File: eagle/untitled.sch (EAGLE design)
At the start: 58 parts, among them J1 JTAG, Q1 16MHz, U1 MMA3202KEG

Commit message: 2nd version in production.
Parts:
- BOOST: value V_REG_TPS61040SMD -> TPS61040
- D13: value DIODE -> MBRA140; device gipi:DIODE -> SparkFun-DiscreteSemi:DIODE-SCHOTTKY-MBRA140
- L1: value (none) -> 3.3uH; device SparkFun-Passives:INDUCTOR0603 -> SparkFun-Passives:INDUCTOR1210
- N-FET: value P-CHANNEL-MOSFET -> N-CHANNEL-MOSFET-BSS138; device GeekAmmo:P-CHANNEL-MOSFET -> GeekAmmo:N-CHANNEL-MOSFET-BSS138
- RA: value 1k -> 3.09k
- renumbered R17 to RA, R18 to RB
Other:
- moved on the sheet: N-FET
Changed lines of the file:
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@@
 <part name="XS" library="SparkFun-LED" deviceset="LED" device="0603"/>
 <part name="GND-ISO13" library="SparkFun-Aesthetics" deviceset="GND-ISO" device=""/>
-<part name="BOOST" library="SparkFun-PowerIC" deviceset="V_REG_TPS61040" device="SMD"/>
-<part name="L1" library="SparkFun-Passives" deviceset="INDUCTOR" device="0603"/>
+<part name="BOOST" library="SparkFun-PowerIC" deviceset="V_REG_TPS61040" device="SMD" value="TPS61040"/>
+<part name="L1" library="SparkFun-Passives" deviceset="INDUCTOR" device="1210" value="3.3uH"/>
 <part name="C7" library="SparkFun-Capacitors" deviceset="CAP" device="0603-CAP" value="10nF"/>
 <part name="GND-ISO14" library="SparkFun-Aesthetics" deviceset="GND-ISO" device=""/>
-<part name="D13" library="gipi" deviceset="DIODE" device=""/>
-<part name="R17" library="SparkFun-Passives" deviceset="RESISTOR" device="0603-RES" value="1k"/>
-<part name="R18" library="SparkFun-Passives" deviceset="RESISTOR" device="0603-RES" value="1k"/>
+<part name="D13" library="SparkFun-DiscreteSemi" deviceset="DIODE-SCHOTTKY" device="-MBRA140" value="MBRA140"/>
+<part name="RA" library="SparkFun-Passives" deviceset="RESISTOR" device="0603-RES" value="3.09k"/>
+<part name="RB" library="SparkFun-Passives" deviceset="RESISTOR" device="0603-RES" value="1k"/>
 <part name="C8" library="SparkFun-Capacitors" deviceset="CAP" device="0603-CAP" value="10nF"/>
 <part name="C9" library="SparkFun-Capacitors" deviceset="CAP" device="0603-CAP" value="10nF"/>
@@
 <part name="GND-ISO2" library="SparkFun-Aesthetics" deviceset="GND-ISO" device=""/>
 <part name="JP6" library="SparkFun-Connectors" deviceset="M02" device="JST-PTH-VERT"/>
-<part name="N-FET" library="GeekAmmo" deviceset="P-CHANNEL-MOSFET" device=""/>
+<part name="N-FET" library="GeekAmmo" deviceset="N-CHANNEL-MOSFET" device="-BSS138"/>
 <part name="TP1" library="gipi" deviceset="TESTPAD" device=""/>
 </parts>
@@
 <instance part="GND-ISO14" gate="G$1" x="88.9" y="-246.38"/>
 <instance part="D13" gate="G$1" x="71.12" y="-205.74"/>
-<instance part="R17" gate="G$1" x="81.28" y="-215.9" rot="R90"/>
-<instance part="R18" gate="G$1" x="76.2" y="-233.68" rot="R90"/>
+<instance part="RA" gate="G$1" x="81.28" y="-215.9" rot="R90"/>
+<instance part="RB" gate="G$1" x="76.2" y="-233.68" rot="R90"/>
 <instance part="C8" gate="G$1" x="99.06" y="-213.36" rot="R180"/>
 <instance part="C9" gate="G$1" x="114.3" y="-226.06" rot="R180"/>
@@
 <instance part="GND-ISO2" gate="G$1" x="-33.02" y="20.32"/>
 <instance part="JP6" gate="G$1" x="-27.94" y="-208.28" rot="R270"/>
-<instance part="N-FET" gate="G$1" x="-15.24" y="-220.98" rot="R90"/>
+<instance part="N-FET" gate="G$1" x="-7.62" y="-228.6"/>
 <instance part="TP1" gate="G$1" x="38.1" y="-134.62" rot="R180"/>
 </instances>
@@
 <wire x1="10.16" y1="-215.9" x2="10.16" y2="-223.52" width="0.1524" layer="91"/>
 <junction x="10.16" y="-215.9"/>
-<wire x1="-5.08" y1="-218.44" x2="-5.08" y2="-205.74" width="0.1524" layer="91"/>
+<wire x1="-5.08" y1="-220.98" x2="-5.08" y2="-205.74" width="0.1524" layer="91"/>
 <wire x1="-5.08" y1="-205.74" x2="10.16" y2="-205.74" width="0.1524" layer="91"/>
 <junction x="10.16" y="-205.74"/>
 <pinref part="N-FET" gate="G$1" pin="D"/>
-<wire x1="-7.62" y1="-218.44" x2="-5.08" y2="-218.44" width="0.1524" layer="91"/>
 </segment>
 </net>
@@
 <wire x1="63.5" y1="-220.98" x2="63.5" y2="-241.3" width="0.1524" layer="91"/>
 <junction x="63.5" y="-241.3"/>
-<pinref part="R18" gate="G$1" pin="1"/>
+<pinref part="RB" gate="G$1" pin="1"/>
 <wire x1="76.2" y1="-238.76" x2="76.2" y2="-241.3" width="0.1524" layer="91"/>
 <junction x="76.2" y="-241.3"/>
@@
 <wire x1="114.3" y1="-241.3" x2="114.3" y2="-231.14" width="0.1524" layer="91"/>
 <junction x="88.9" y="-241.3"/>
-<wire x1="-25.4" y1="-241.3" x2="-17.78" y2="-241.3" width="0.1524" layer="91"/>
+<wire x1="-25.4" y1="-241.3" x2="-12.7" y2="-241.3" width="0.1524" layer="91"/>
 <junction x="10.16" y="-241.3"/>
 <pinref part="JP6" gate="G$1" pin="2"/>
-<wire x1="-17.78" y1="-241.3" x2="10.16" y2="-241.3" width="0.1524" layer="91"/>
+<wire x1="-12.7" y1="-241.3" x2="10.16" y2="-241.3" width="0.1524" layer="91"/>
 <wire x1="-25.4" y1="-215.9" x2="-25.4" y2="-241.3" width="0.1524" layer="91"/>
 <pinref part="N-FET" gate="G$1" pin="G"/>
-<wire x1="-17.78" y1="-226.06" x2="-17.78" y2="-241.3" width="0.1524" layer="91"/>
-<junction x="-17.78" y="-241.3"/>
+<wire x1="-12.7" y1="-231.14" x2="-12.7" y2="-241.3" width="0.1524" layer="91"/>
+<junction x="-12.7" y="-241.3"/>
 </segment>
 <segment>
@@
 <pinref part="BOOST" gate="G$1" pin="FB"/>
 <wire x1="45.72" y1="-226.06" x2="76.2" y2="-226.06" width="0.1524" layer="91"/>
-<pinref part="R18" gate="G$1" pin="2"/>
+<pinref part="RB" gate="G$1" pin="2"/>
 <wire x1="76.2" y1="-226.06" x2="81.28" y2="-226.06" width="0.1524" layer="91"/>
 <wire x1="81.28" y1="-226.06" x2="99.06" y2="-226.06" width="0.1524" layer="91"/>
 <wire x1="76.2" y1="-228.6" x2="76.2" y2="-226.06" width="0.1524" layer="91"/>
 <junction x="76.2" y="-226.06"/>
-<pinref part="R17" gate="G$1" pin="1"/>
+<pinref part="RA" gate="G$1" pin="1"/>
 <wire x1="81.28" y1="-220.98" x2="81.28" y2="-226.06" width="0.1524" layer="91"/>
 <junction x="81.28" y="-226.06"/>
@@
 <pinref part="D13" gate="G$1" pin="C"/>
 <wire x1="99.06" y1="-205.74" x2="81.28" y2="-205.74" width="0.1524" layer="91"/>
-<pinref part="R17" gate="G$1" pin="2"/>
+<pinref part="RA" gate="G$1" pin="2"/>
 <wire x1="81.28" y1="-205.74" x2="73.66" y2="-205.74" width="0.1524" layer="91"/>
 <wire x1="81.28" y1="-210.82" x2="81.28" y2="-205.74" width="0.1524" layer="91"/>
@@
 <segment>
 <pinref part="JP6" gate="G$1" pin="1"/>
-<wire x1="-27.94" y1="-215.9" x2="-27.94" y2="-218.44" width="0.1524" layer="91"/>
+<wire x1="-27.94" y1="-215.9" x2="-27.94" y2="-236.22" width="0.1524" layer="91"/>
 <pinref part="N-FET" gate="G$1" pin="S"/>
-<wire x1="-27.94" y1="-218.44" x2="-22.86" y2="-218.44" width="0.1524" layer="91"/>
-</segment>
-</net>
+<wire x1="-27.94" y1="-236.22" x2="-5.08" y2="-236.22" width="0.1524" layer="91"/>
+</segment>
+</net>

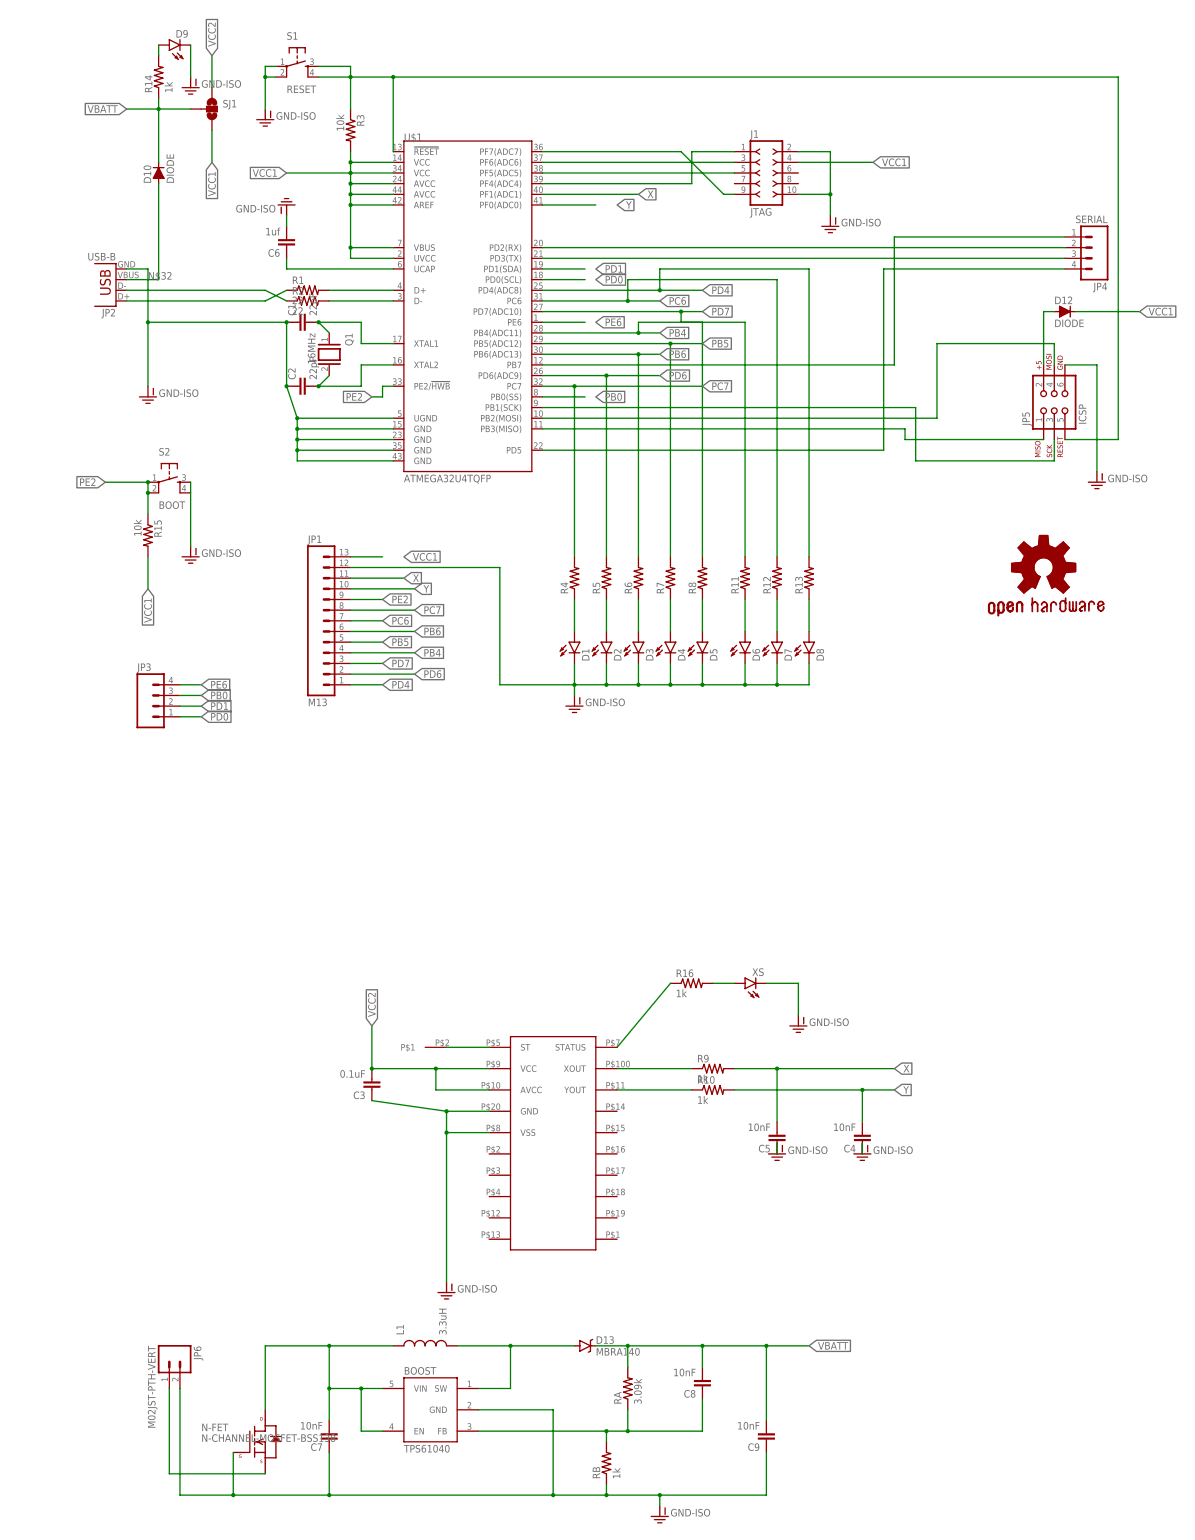
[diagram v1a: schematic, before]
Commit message: Fix mess with ground.
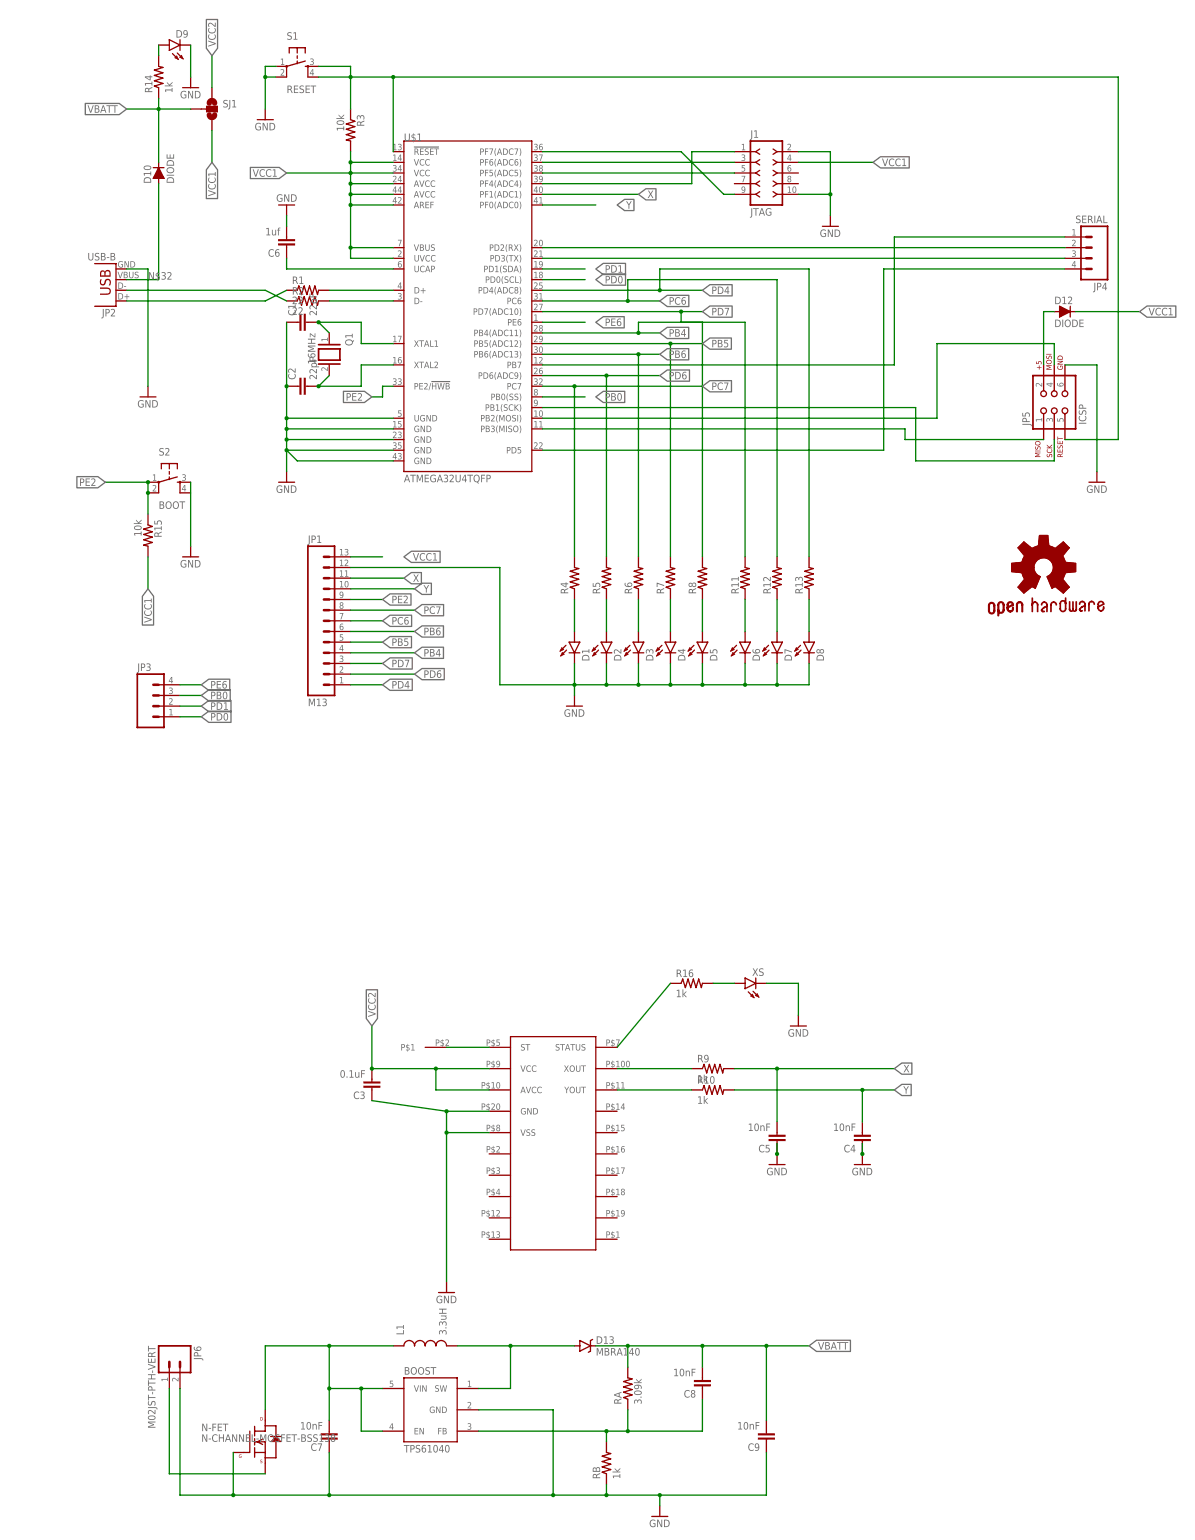
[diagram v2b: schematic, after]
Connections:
- removed net GN: C4.1, C5.1, C6.2, D1.C, D2.C, D3.C, D4.C, D5.C, D6.C, D7.C, D8.C, D9.C, J1.10, J1.2, JP1.12, JP5.6, S1.1, S1.2, S2.3, XS.C
- removed net GND-ISO: BOOST.GND, C1.1, C2.1, C3.1, C7.1, C9.1, JP2.GND, JP6.2, N-FET.G, RB.1, U$1.GND@15, U$1.GND@23, U$1.GND@35, U$1.GND@43, U$1.UGND, U1.GND, U1.VSS
- new net GND: BOOST.GND, C1.1, C2.1, C3.1, C4.1, C5.1, C6.2, C7.1, C9.1, D1.C, D2.C, D3.C, D4.C, D5.C, D6.C, D7.C, D8.C, D9.C, J1.10, J1.2, JP1.12, JP2.GND, JP5.6, JP6.2, N-FET.G, RB.1, S1.1, S1.2, S2.3, U$1.GND@15, U$1.GND@23, U$1.GND@35, U$1.GND@43, U$1.UGND, U1.GND, U1.VSS, XS.C

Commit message: Update ciaoduino's eagle files.
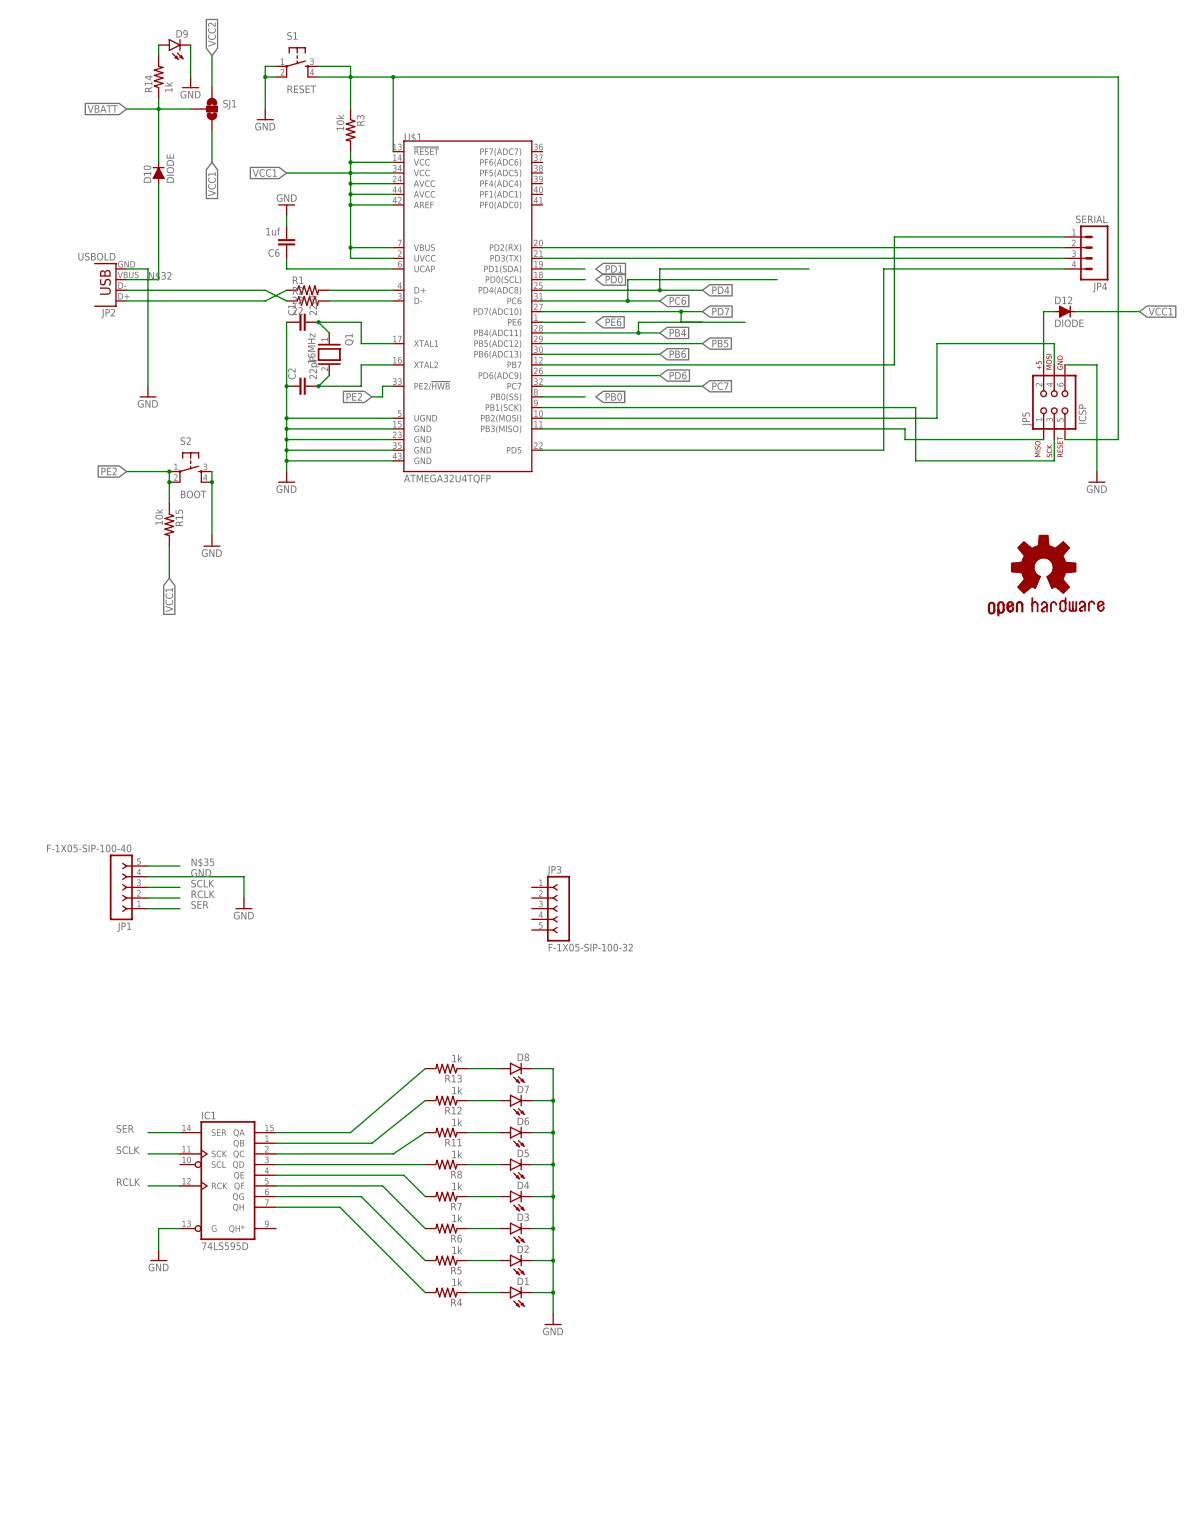
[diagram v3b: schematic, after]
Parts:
- removed BOOST: TPS61040, SparkFun-PowerIC:V_REG_TPS61040SMD
- removed C3: 0.1uF, SparkFun-Capacitors:CAP0603-CAP
- removed C4, C5, C7, C8, C9: 10nF, SparkFun-Capacitors:CAP0603-CAP
- removed D13: MBRA140, SparkFun-DiscreteSemi:DIODE-SCHOTTKY-MBRA140
- removed J1: JTAG, con-headers-jp:F-2X05-DIL-2MM
- removed JP6: M02JST-PTH-VERT, SparkFun-Connectors:M02JST-PTH-VERT
- removed L1: 3.3uH, SparkFun-Passives:INDUCTOR1210
- removed N-FET: N-CHANNEL-MOSFET-BSS138, GeekAmmo:N-CHANNEL-MOSFET-BSS138
- removed R10, R16, R9, RB: 1k, SparkFun-Passives:RESISTOR0603-RES
- removed RA: 3.09k, SparkFun-Passives:RESISTOR0603-RES
- removed TP1: TESTPAD, gipi:TESTPAD
- removed U1: MMA3202KEG, gipi:MMA3202KEG
- removed XS: (no value), SparkFun-LED:LED0603
- added IC1: 74LS595D, 74xx-us:74LS595D
- C6: device eagle-ltspice:CC1206 -> eagle-ltspice:CC0603
- JP1: value M13 -> F-1X05-SIP-100-40; device SparkFun-Connectors:M13 -> con-headers-jp:F-1X05-SIP-100-40
- JP2: value USB-B -> USBOLD; device SparkFun-Connectors:USBPTH -> SparkFun-Connectors:USBOLD
- JP3: value (none) -> F-1X05-SIP-100-32; device SparkFun-Connectors:M04PTH -> con-headers-jp:F-1X05-SIP-100-32
- R1, R2: device SparkFun-Passives:RESISTOR1206 -> SparkFun-Passives:RESISTOR0603-RES
- R11, R12, R13, R4, R5, R6, R7, R8: value (none) -> 1k; device SparkFun-Passives:RESISTOR1206 -> SparkFun-Passives:RESISTOR0603-RES
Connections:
- removed net N$36: R16.2, XS.A
- removed net N$38: BOOST.EN, BOOST.VIN, C7.2, L1.1, N-FET.D
- removed net N$39: BOOST.SW, D13.A, L1.2
- removed net N$41: BOOST.FB, C8.1, RA.1, RB.2
- removed net X: C5.2, JP1.11, R9.2, U$1.PF1(ADC1)
- removed net Y: C4.2, JP1.10, R10.2, U$1.PF0(ADC0)
- new net RCLK: IC1A.RCK, JP1.2
- new net SCLK: IC1A.SCK, JP1.3
- new net SER: IC1A.SER, JP1.1
- net GND: now also IC1A.G, JP1.4, S2.4; no longer BOOST.GND, C3.1, C4.1, C5.1, C7.1, C9.1, J1.10, J1.2, JP1.12, JP6.2, N-FET.G, RB.1, U1.GND, U1.VSS, XS.C
- net N$1: now also IC1A.QA, R13.2; no longer R9.1, U1.XOUT
- net N$21: now also IC1A.QB, R12.2; no longer R10.1, U1.YOUT
- net N$22: now also IC1A.QC, R11.2; no longer J1.1, U$1.PF4(ADC4)
- net N$25: now also IC1A.QD, R8.2; no longer J1.5, U$1.PF5(ADC5)
- net N$26: now also IC1A.QE, R7.2; no longer J1.3, U$1.PF6(ADC6)
- net N$27: now also IC1A.QF, R6.2; no longer J1.9, U$1.PF7(ADC7)
- net N$28: now also IC1A.QG, R5.2; no longer TP1.P$1, U1.ST
- net N$33: now also IC1A.QH, R4.2; no longer JP6.1, N-FET.S
- net N$35: now also JP1.5; no longer R16.1, U1.STATUS
- net PB0: no longer JP3.3
- net PB4: no longer JP1.4, R8.2
- net PB5: no longer JP1.5, R7.2
- net PB6: no longer JP1.6, R6.2
- net PC6: no longer JP1.7, R12.2
- net PC7: no longer JP1.8, R4.2
- net PD0: no longer JP3.1
- net PD1: no longer JP3.2
- net PD4: no longer JP1.1, R13.2
- net PD6: no longer JP1.2, R5.2
- net PD7: no longer JP1.3, R11.2
- net PE2: no longer JP1.9
- net PE6: no longer JP3.4
- net VBATT: no longer C8.2, C9.2, D13.C, RA.2
- net VCC1: no longer J1.4, JP1.13
- net VCC2: no longer C3.2, U1.AVCC, U1.VCC
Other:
- moved on the sheet: D1, D2, D3, D4, D5, D6, D7, D8, R11, R12, R13, R15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
